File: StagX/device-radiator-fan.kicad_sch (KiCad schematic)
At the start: 2 parts

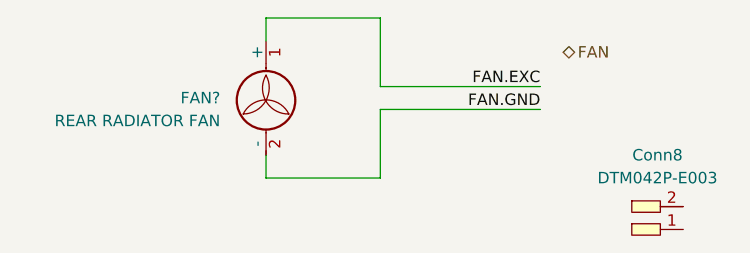
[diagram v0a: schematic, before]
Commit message: Completed shutdown loop
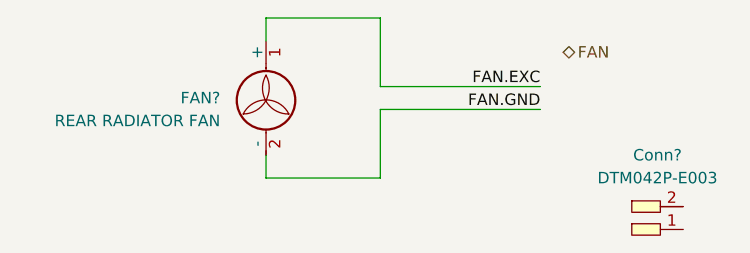
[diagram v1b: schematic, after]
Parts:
- renumbered Conn8 to Conn?
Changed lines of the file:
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@@
   (symbol (lib_id "Connectors_SUFST:Deutsch_DTM_2P_Pin") (at 179.07 99.06 0) (unit 1)
     (in_bom yes) (on_board yes) (dnp no) (fields_autoplaced)
-    (property "Reference" "Conn8" (at 178.1175 97.79 0)
+    (property "Reference" "Conn?" (at 178.1175 97.79 0)
       (effects (font (size 1.27 1.27)))
     )
@@
       (project "StagX"
         (path "/03011643-0690-4b85-ab78-d6a62dae52b1/808d560b-b52c-4c85-927c-da1ea855555d"
-          (reference "Conn8") (unit 1)
+          (reference "Conn?") (unit 1)
         )
       )
